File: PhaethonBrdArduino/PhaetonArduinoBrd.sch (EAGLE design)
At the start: 40 parts, among them IC2 LM2596S, Q1 32.768 Hz, SW1 EC12E_SW

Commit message: Issue: Change the RGB LED #1
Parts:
- added R12: 230, SparkFun:RESISTOR
- added R13: 90, SparkFun:RESISTOR
- LED: value GM5WA94310A -> WL-SFTW-150141M173100-R&G&B; device led:GM5WA94310A -> Wuerth_Elektronik_LEDs_rev15b:WL-SFTW-150141M173100-R&G&B
- R11: value 10K\ -> 125
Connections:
- removed net N$11: LEDB.C, LEDG.C, LEDR.C, R11.2
- new net N$1: LED.BC, R11.1
- new net N$2: LED.RC, R12.1
- new net N$3: LED.GC, R13.1
- net +5V: now also LED.A
- net A0: now also R11.2; no longer LEDB.A
- net A1: now also R13.2; no longer LEDR.A
- net A2: now also R12.2; no longer LEDG.A
- net GND: no longer R11.1
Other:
- moved on the sheet: R11
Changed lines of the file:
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@@
 <part name="C2" library="rcl" deviceset="C-EU" device="C0805K" value="100nF"/>
 <part name="GND11" library="supply1" deviceset="GND" device=""/>
-<part name="LED" library="led" deviceset="GM5WA94310A" device="" value=""/>
 <part name="T1" library="transistor" deviceset="*-NPN-" device="SOT23-BEC" technology="BC818-16"/>
 <part name="GND12" library="supply1" deviceset="GND" device=""/>
@@
 <part name="GND16" library="supply1" deviceset="GND" device=""/>
 <part name="SV1" library="con-amp-mt6" deviceset="MT6-3" device=""/>
-<part name="R11" library="SparkFun" deviceset="RESISTOR" device="" value="10K\"/>
-<part name="GND17" library="supply1" deviceset="GND" device=""/>
+<part name="R11" library="SparkFun" deviceset="RESISTOR" device="" value="125"/>
 <part name="DISPLAYCONNECTOR" library="con-amp-quick" deviceset="M04" device=""/>
 <part name="GND18" library="supply1" deviceset="GND" device=""/>
 <part name="GND19" library="supply1" deviceset="GND" device=""/>
 <part name="L1" library="inductor-coilcraft" deviceset="MSS1260" device="" value="68uH"/>
+<part name="LED" library="Wuerth_Elektronik_LEDs_rev15b" deviceset="WL-SFTW" device="-150141M173100-R&amp;G&amp;B"/>
+<part name="P+14" library="supply1" deviceset="+5V" device=""/>
+<part name="R12" library="SparkFun" deviceset="RESISTOR" device="" value="230"/>
+<part name="R13" library="SparkFun" deviceset="RESISTOR" device="" value="90"/>
 </parts>
 <sheets>
@@
 <instance part="C2" gate="G$1" x="279.4" y="15.24"/>
 <instance part="GND11" gate="1" x="279.4" y="5.08"/>
-<instance part="LED" gate="R" x="101.6" y="99.06" rot="R180"/>
-<instance part="LED" gate="G" x="88.9" y="99.06" rot="R180"/>
-<instance part="LED" gate="B" x="76.2" y="99.06" rot="R180"/>
 <instance part="T1" gate="G$1" x="226.06" y="27.94"/>
 <instance part="GND12" gate="1" x="228.6" y="10.16"/>
@@
 <instance part="SV1" gate="-2" x="149.86" y="-12.7" rot="R270"/>
 <instance part="SV1" gate="-3" x="144.78" y="-12.7" rot="R270"/>
-<instance part="R11" gate="G$1" x="81.28" y="111.76" rot="R180"/>
-<instance part="GND17" gate="1" x="93.98" y="111.76" rot="R90"/>
+<instance part="R11" gate="G$1" x="78.74" y="93.98" rot="R270"/>
 <instance part="DISPLAYCONNECTOR" gate="G$1" x="195.58" y="-15.24" rot="R270"/>
 <instance part="GND18" gate="1" x="203.2" y="93.98" rot="R90"/>
 <instance part="GND19" gate="1" x="203.2" y="86.36" rot="R90"/>
 <instance part="L1" gate="G$1" x="73.66" y="-27.94" rot="R90"/>
+<instance part="LED" gate="G$1" x="86.36" y="106.68" smashed="yes" rot="R270">
+<attribute name="NAME" x="98.202" y="110.37" size="1.27" layer="95" rot="R270"/>
+<attribute name="VALUE" x="90.29" y="118.112" size="1.27" layer="96"/>
+</instance>
+<instance part="P+14" gate="1" x="86.36" y="124.46"/>
+<instance part="R12" gate="G$1" x="86.36" y="93.98" rot="R270"/>
+<instance part="R13" gate="G$1" x="93.98" y="93.98" rot="R270"/>
 </instances>
 <busses>
@@
 <wire x1="193.04" y1="-20.32" x2="193.04" y2="-25.4" width="0.1524" layer="91"/>
 <label x="193.04" y="-25.4" size="1.778" layer="95" rot="R90"/>
+</segment>
+<segment>
+<pinref part="LED" gate="G$1" pin="A"/>
+<pinref part="P+14" gate="1" pin="+5V"/>
+<wire x1="86.36" y1="116.84" x2="86.36" y2="121.92" width="0.1524" layer="91"/>
 </segment>
 </net>
@@
 <wire x1="149.86" y1="-17.78" x2="149.86" y2="-25.4" width="0.1524" layer="91"/>
 <label x="149.86" y="-27.94" size="1.778" layer="95" rot="R90"/>
-</segment>
-<segment>
-<pinref part="R11" gate="G$1" pin="1"/>
-<pinref part="GND17" gate="1" pin="GND"/>
-<wire x1="91.44" y1="111.76" x2="86.36" y2="111.76" width="0.1524" layer="91"/>
 </segment>
 <segment>
@@
 </segment>
 </net>
-<net name="N$11" class="0">
-<segment>
-<pinref part="LED" gate="B" pin="C"/>
-<pinref part="R11" gate="G$1" pin="2"/>
-<wire x1="76.2" y1="104.14" x2="76.2" y2="106.68" width="0.1524" layer="91"/>
-<pinref part="LED" gate="G" pin="C"/>
-<wire x1="76.2" y1="106.68" x2="76.2" y2="111.76" width="0.1524" layer="91"/>
-<wire x1="88.9" y1="104.14" x2="88.9" y2="106.68" width="0.1524" layer="91"/>
-<wire x1="88.9" y1="106.68" x2="76.2" y2="106.68" width="0.1524" layer="91"/>
-<wire x1="88.9" y1="106.68" x2="101.6" y2="106.68" width="0.1524" layer="91"/>
-<pinref part="LED" gate="R" pin="C"/>
-<wire x1="101.6" y1="106.68" x2="101.6" y2="104.14" width="0.1524" layer="91"/>
-<junction x="76.2" y="106.68"/>
-<junction x="88.9" y="106.68"/>
-<junction x="101.6" y="106.68"/>
-</segment>
-</net>
 <net name="A0" class="0">
-<segment>
-<pinref part="LED" gate="B" pin="A"/>
-<wire x1="76.2" y1="96.52" x2="76.2" y2="88.9" width="0.1524" layer="91"/>
-<label x="76.2" y="83.82" size="1.778" layer="95"/>
-</segment>
 <segment>
 <wire x1="129.54" y1="53.34" x2="119.38" y2="53.34" width="0.1524" layer="91"/>
@@
 <pinref part="J6" gate="A" pin="1"/>
 </segment>
+<segment>
+<pinref part="R11" gate="G$1" pin="2"/>
+<wire x1="78.74" y1="88.9" x2="78.74" y2="86.36" width="0.1524" layer="91"/>
+<label x="78.74" y="86.36" size="1.778" layer="95"/>
+</segment>
 </net>
 <net name="A1" class="0">
-<segment>
-<pinref part="LED" gate="R" pin="A"/>
-<wire x1="101.6" y1="96.52" x2="101.6" y2="88.9" width="0.1524" layer="91"/>
-<label x="101.6" y="83.82" size="1.778" layer="95"/>
-</segment>
 <segment>
 <wire x1="129.54" y1="50.8" x2="119.38" y2="50.8" width="0.1524" layer="91"/>
@@
 <pinref part="J6" gate="A" pin="2"/>
 </segment>
+<segment>
+<pinref part="R13" gate="G$1" pin="2"/>
+<wire x1="93.98" y1="88.9" x2="93.98" y2="86.36" width="0.1524" layer="91"/>
+<label x="93.98" y="86.36" size="1.778" layer="95"/>
+</segment>
 </net>
 <net name="A2" class="0">
-<segment>
-<pinref part="LED" gate="G" pin="A"/>
-<wire x1="88.9" y1="96.52" x2="88.9" y2="88.9" width="0.1524" layer="91"/>
-<label x="88.9" y="83.82" size="1.778" layer="95"/>
-</segment>
 <segment>
 <wire x1="129.54" y1="48.26" x2="119.38" y2="48.26" width="0.1524" layer="91"/>
 <pinref part="ANALOG" gate="A" pin="3"/>
 <pinref part="J6" gate="A" pin="3"/>
+</segment>
+<segment>
+<pinref part="R12" gate="G$1" pin="2"/>
+<wire x1="86.36" y1="88.9" x2="86.36" y2="86.36" width="0.1524" layer="91"/>
+<label x="86.36" y="86.36" size="1.778" layer="95"/>
 </segment>
 </net>
@@
 </segment>
 </net>
+<net name="N$1" class="0">
+<segment>
+<pinref part="R11" gate="G$1" pin="1"/>
+<pinref part="LED" gate="G$1" pin="BC"/>
+<wire x1="78.74" y1="99.06" x2="78.74" y2="101.6" width="0.1524" layer="91"/>
+</segment>
+</net>
+<net name="N$2" class="0">
+<segment>
+<pinref part="R12" gate="G$1" pin="1"/>
+<pinref part="LED" gate="G$1" pin="RC"/>
+<wire x1="86.36" y1="99.06" x2="86.36" y2="101.6" width="0.1524" layer="91"/>
+</segment>
+</net>
+<net name="N$3" class="0">
+<segment>
+<pinref part="R13" gate="G$1" pin="1"/>
+<pinref part="LED" gate="G$1" pin="GC"/>
+<wire x1="93.98" y1="99.06" x2="93.98" y2="101.6" width="0.1524" layer="91"/>
+</segment>
+</net>

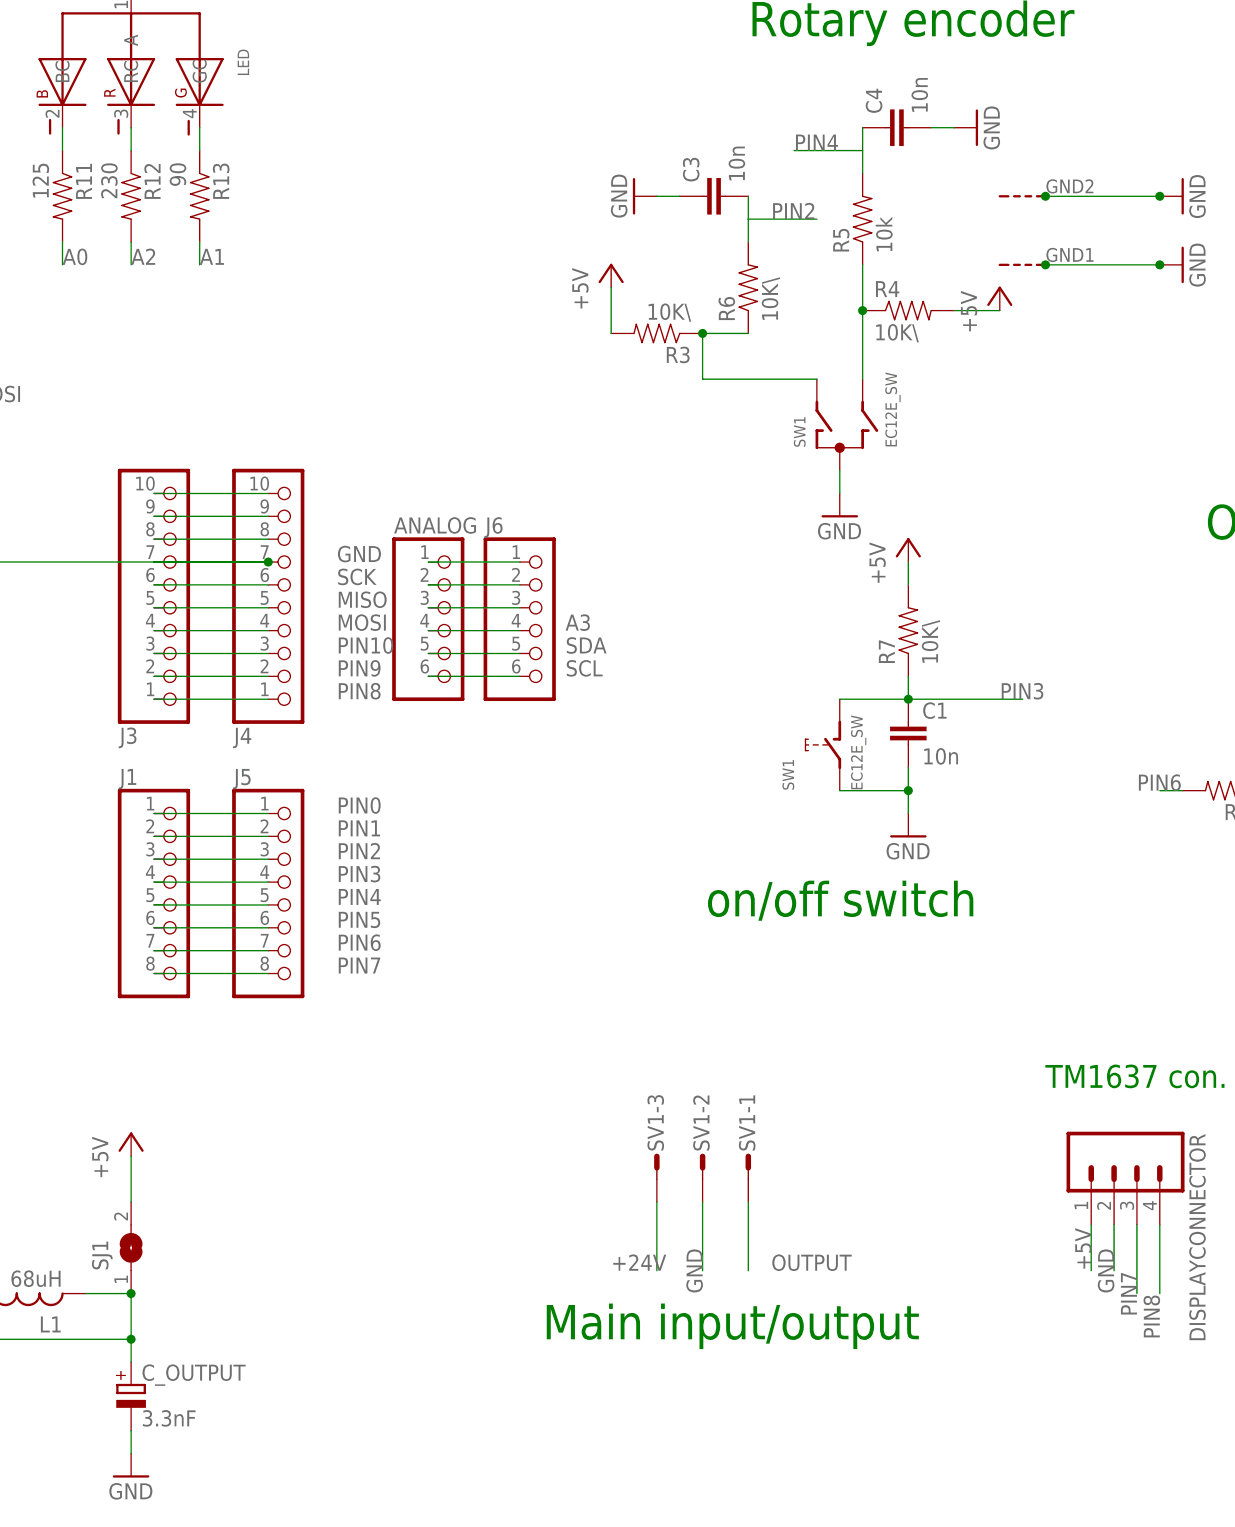
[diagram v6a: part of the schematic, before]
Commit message: Added bridge, Issue #3
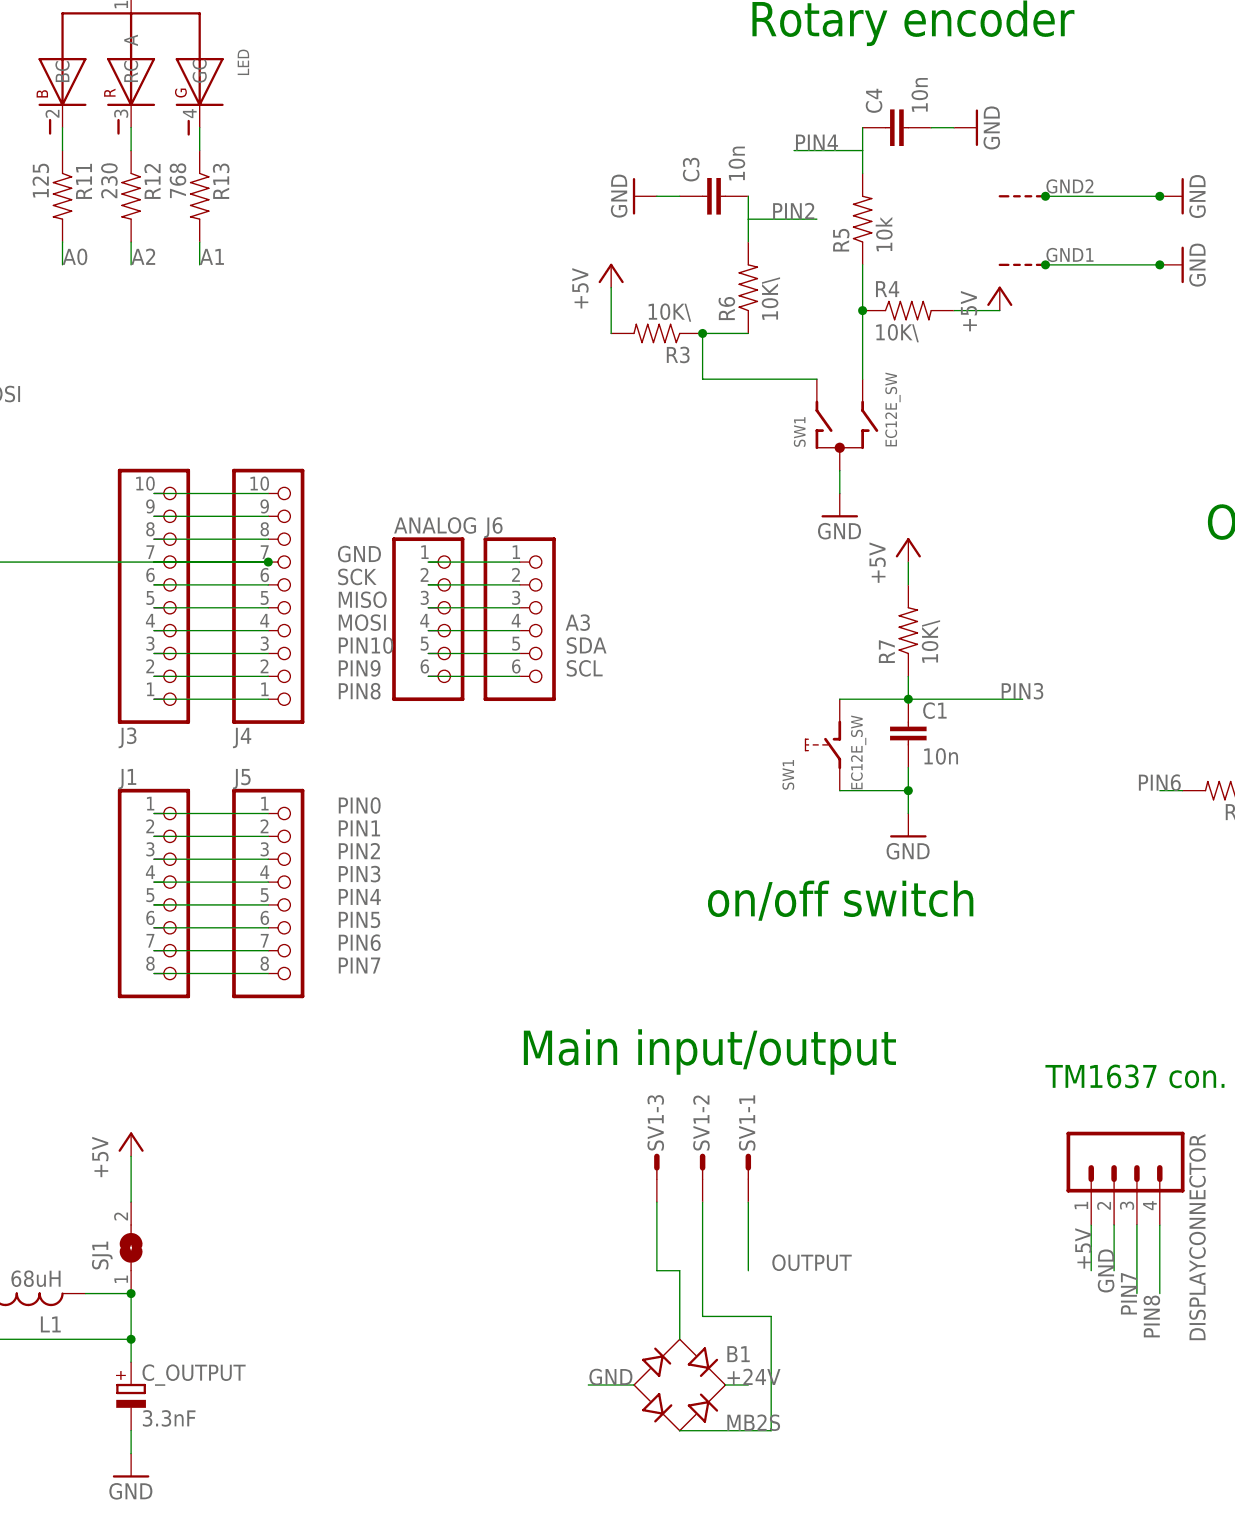
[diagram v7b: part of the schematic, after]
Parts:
- added B1: MB2S, rectifier:MB2S
- R13: value 90 -> 768
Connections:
- new net N$4: B1.AC1, SV1-3.S
- new net N$6: B1.AC2, SV1-2.S
- net +24V: now also B1.+; no longer SV1-3.S
- net GND: now also B1.-; no longer SV1-2.S
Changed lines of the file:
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@@
 <part name="P+14" library="supply1" deviceset="+5V" device=""/>
 <part name="R12" library="SparkFun" deviceset="RESISTOR" device="" value="230"/>
-<part name="R13" library="SparkFun" deviceset="RESISTOR" device="" value="90"/>
+<part name="R13" library="SparkFun" deviceset="RESISTOR" device="" value="768"/>
+<part name="B1" library="rectifier" deviceset="MB*S" device="" technology="2"/>
 </parts>
 <sheets>
@@
 <text x="66.04" y="88.9" size="2.54" layer="91" rot="R90">RGB LED</text>
 <text x="180.34" y="17.78" size="3.81" layer="91" rot="R180">on/off switch</text>
-<text x="132.08" y="-33.02" size="3.81" layer="91">Main input/output</text>
+<text x="129.54" y="-2.54" size="3.81" layer="91">Main input/output</text>
 <text x="187.96" y="-5.08" size="2.54" layer="91">TM1637 con.</text>
 <text x="205.74" y="55.88" size="3.81" layer="91">Output controller</text>
@@
 <instance part="R12" gate="G$1" x="86.36" y="93.98" rot="R270"/>
 <instance part="R13" gate="G$1" x="93.98" y="93.98" rot="R270"/>
+<instance part="B1" gate="G$1" x="147.32" y="-38.1"/>
 </instances>
 <busses>
@@
 </segment>
 <segment>
-<pinref part="SV1" gate="-2" pin="S"/>
-<wire x1="149.86" y1="-17.78" x2="149.86" y2="-25.4" width="0.1524" layer="91"/>
-<label x="149.86" y="-27.94" size="1.778" layer="95" rot="R90"/>
-</segment>
-<segment>
 <pinref part="DISPLAYCONNECTOR" gate="G$1" pin="2"/>
 <wire x1="195.58" y1="-20.32" x2="195.58" y2="-25.4" width="0.1524" layer="91"/>
@@
 <junction x="187.96" y="93.98"/>
 <junction x="200.66" y="93.98"/>
+</segment>
+<segment>
+<pinref part="B1" gate="G$1" pin="-"/>
+<wire x1="142.24" y1="-38.1" x2="137.16" y2="-38.1" width="0.1524" layer="91"/>
+<label x="137.16" y="-38.1" size="1.778" layer="95"/>
 </segment>
 </net>
@@
 </segment>
 <segment>
-<pinref part="SV1" gate="-3" pin="S"/>
-<wire x1="144.78" y1="-17.78" x2="144.78" y2="-25.4" width="0.1524" layer="91"/>
-<label x="139.7" y="-25.4" size="1.778" layer="95"/>
+<pinref part="B1" gate="G$1" pin="+"/>
+<wire x1="152.4" y1="-38.1" x2="154.94" y2="-38.1" width="0.1524" layer="91"/>
+<label x="152.4" y="-38.1" size="1.778" layer="95"/>
 </segment>
 </net>
@@
 </segment>
 </net>
+<net name="N$4" class="0">
+<segment>
+<pinref part="B1" gate="G$1" pin="AC1"/>
+<wire x1="147.32" y1="-33.02" x2="147.32" y2="-25.4" width="0.1524" layer="91"/>
+<wire x1="147.32" y1="-25.4" x2="144.78" y2="-25.4" width="0.1524" layer="91"/>
+<pinref part="SV1" gate="-3" pin="S"/>
+<wire x1="144.78" y1="-25.4" x2="144.78" y2="-17.78" width="0.1524" layer="91"/>
+</segment>
+</net>
+<net name="N$6" class="0">
+<segment>
+<pinref part="B1" gate="G$1" pin="AC2"/>
+<wire x1="147.32" y1="-43.18" x2="157.48" y2="-43.18" width="0.1524" layer="91"/>
+<wire x1="157.48" y1="-43.18" x2="157.48" y2="-30.48" width="0.1524" layer="91"/>
+<wire x1="157.48" y1="-30.48" x2="149.86" y2="-30.48" width="0.1524" layer="91"/>
+<pinref part="SV1" gate="-2" pin="S"/>
+<wire x1="149.86" y1="-30.48" x2="149.86" y2="-17.78" width="0.1524" layer="91"/>
+</segment>
+</net>
